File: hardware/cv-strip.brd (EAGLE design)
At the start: 152.5 x 43.6 mm, 118 parts, among them IC1 PIC16F1825SO14, IC2 AD5696R, IC3 MC14094B, IC4 MC14094B, IC5 LM324D, IC6 REG1117, IC7 6N138

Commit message: Final rev 2 release PCB
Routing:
- net GND: vias 7 -> 8
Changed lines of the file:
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@@
 </class>
 </classes>
-<designrules name="ITEADstudio_DRC">
-<description language="de">&lt;b&gt;EAGLE Design Rules&lt;/b&gt;
-&lt;p&gt;
-Die Standard-Design-Rules sind so gewählt, dass sie für
-die meisten Anwendungen passen. Sollte ihre Platine
-besondere Anforderungen haben, treffen Sie die erforderlichen
-Einstellungen hier und speichern die Design Rules unter
-einem neuen Namen ab.</description>
-<description language="en">&lt;b&gt;EAGLE Design Rules&lt;/b&gt;
-&lt;p&gt;
-The default Design Rules have been set to cover
-a wide range of applications. Your particular design
-may have different requirements, so please make the
-necessary adjustments and save your customized
-design rules under a new name.</description>
-<description language="zh">&lt;b&gt;Seeed Studio EAGLE Design Rules&lt;/b&gt;
-</description>
+<designrules name="dirt_cheap_dirty_boards.v1">
+<description language="en">&lt;b&gt;Dirty Cheap Dirty Board Design Rules&lt;/b&gt;
+&lt;br&gt;
+&lt;br&gt;Min width/Spacing: 5/5mil
+&lt;br&gt;Min diameter of finished hole 12mil</description>
 <param name="layerSetup" value="(1*16)"/>
-<param name="mtCopper" value="0.035mm 0.035mm 0.035mm 0.035mm 0.035mm 0.035mm 0.035mm 0.035mm 0.035mm 0.035mm 0.035mm 0.035mm 0.035mm 0.035mm 0.035mm 0.035mm"/>
-<param name="mtIsolate" value="1.5mm 0.15mm 0.2mm 0.15mm 0.2mm 0.15mm 0.2mm 0.15mm 0.2mm 0.15mm 0.2mm 0.15mm 0.2mm 0.15mm 0.2mm"/>
-<param name="mdWireWire" value="6mil"/>
-<param name="mdWirePad" value="6mil"/>
-<param name="mdWireVia" value="6mil"/>
-<param name="mdPadPad" value="6mil"/>
-<param name="mdPadVia" value="6mil"/>
-<param name="mdViaVia" value="6mil"/>
+<param name="mtCopper" value="0.035mm 0.0175mm 0.035mm 0.035mm 0.035mm 0.035mm 0.035mm 0.035mm 0.035mm 0.035mm 0.035mm 0.035mm 0.035mm 0.035mm 0.0175mm 0.035mm"/>
+<param name="mtIsolate" value="1.5mm 1.1mm 0.2mm 0.15mm 0.2mm 0.15mm 0.2mm 0.15mm 0.2mm 0.15mm 0.2mm 0.15mm 0.2mm 0.15mm 0.2mm"/>
+<param name="mdWireWire" value="5mil"/>
+<param name="mdWirePad" value="5mil"/>
+<param name="mdWireVia" value="5mil"/>
+<param name="mdPadPad" value="5mil"/>
+<param name="mdPadVia" value="5mil"/>
+<param name="mdViaVia" value="5mil"/>
 <param name="mdSmdPad" value="0mil"/>
 <param name="mdSmdVia" value="0mil"/>
@@
 <param name="mdDrill" value="10mil"/>
 <param name="mdSmdStop" value="0mil"/>
-<param name="msWidth" value="6mil"/>
+<param name="msWidth" value="5mil"/>
 <param name="msDrill" value="12mil"/>
 <param name="msMicroVia" value="12mil"/>
@@
 <param name="mlMinCreamFrame" value="0mil"/>
 <param name="mlMaxCreamFrame" value="0mil"/>
-<param name="mlViaStopLimit" value="100mil"/>
+<param name="mlViaStopLimit" value="25mil"/>
 <param name="srRoundness" value="0"/>
 <param name="srMinRoundness" value="0mil"/>
@@
 <wire x1="66.675" y1="26.7995" x2="68.0525" y2="26.7995" width="0.4064" layer="16"/>
 <wire x1="68.0525" y1="26.7995" x2="69.088" y2="27.327" width="0.4064" layer="16"/>
-<wire x1="91.302" y1="14.49" x2="93.102" y2="15.99" width="0" layer="19" extent="16-16"/>
-<wire x1="98.944" y1="15.99" x2="97.144" y2="14.49" width="0" layer="19" extent="16-16"/>
+<via x="98.8695" y="18.161" extent="1-16" drill="0.6"/>
 </signal>
 <signal name="MIDI_IN">
@@
 <via x="49.53" y="33.02" extent="1-16" drill="0.6"/>
 <contactref element="C16" pad="+"/>
-<wire x1="60.35" y1="31.9405" x2="64.0105" y2="31.9405" width="0.3048" layer="16"/>
+<wire x1="60.35" y1="31.9405" x2="63.5" y2="31.9405" width="0.3048" layer="16"/>
+<wire x1="64.008" y1="31.9405" x2="64.0105" y2="31.9405" width="0.3048" layer="16"/>
 <wire x1="64.0715" y1="32.004" x2="64.0715" y2="30.9245" width="0.6096" layer="16"/>
 <wire x1="64.0715" y1="30.9245" x2="64.5795" y2="30.4165" width="0.6096" layer="16"/>
@@
 <wire x1="138.43" y1="7.112" x2="137.342" y2="7.112" width="0.6096" layer="16"/>
 <wire x1="137.342" y1="7.112" x2="137.16" y2="6.93" width="0.6096" layer="16"/>
-<wire x1="64.008" y1="31.9405" x2="64.0105" y2="31.9405" width="0" layer="19" extent="16-16"/>
+<wire x1="64.008" y1="31.9405" x2="63.5" y2="31.9405" width="0.4064" layer="16"/>
 </signal>
 <signal name="VIN">

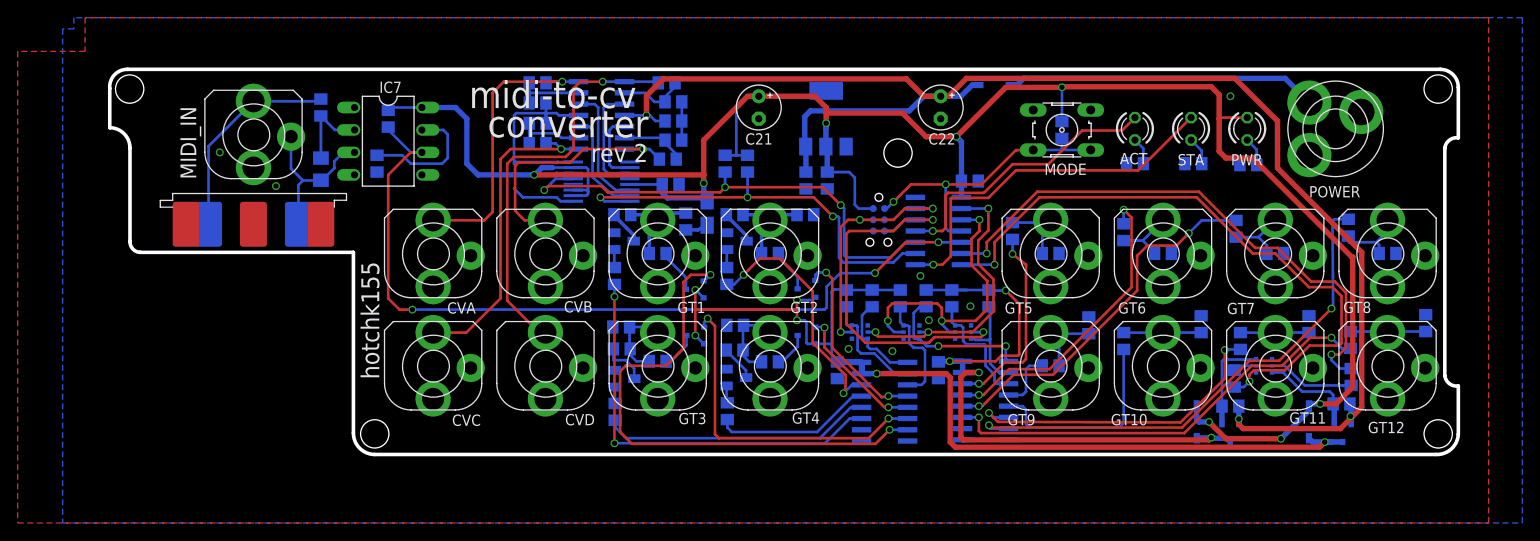
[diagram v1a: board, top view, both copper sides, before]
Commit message: REV2A
fixed some DRC issues
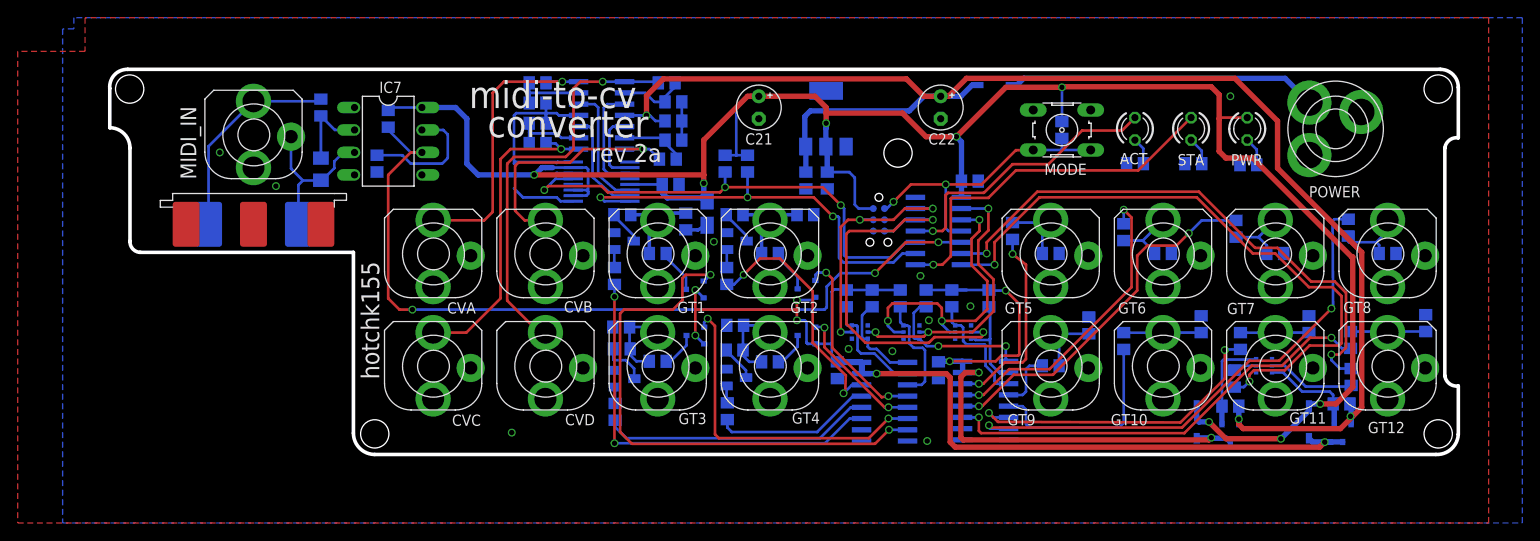
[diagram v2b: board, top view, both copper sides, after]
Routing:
- net GT1H: track 60.8 -> 61.7 mm
- net GND: vias 8 -> 11
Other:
- board text added: "rev 2a"
- board text removed: "rev 2"
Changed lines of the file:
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@@
 <text x="42.164" y="40.5765" size="3.048" layer="25" font="vector">midi-to-cv </text>
 <text x="44.2595" y="37.2745" size="3.048" layer="25" font="vector">converter</text>
-<text x="55.9435" y="34.4805" size="2.032" layer="25" font="vector">rev 2</text>
+<text x="55.9435" y="34.4805" size="2.032" layer="25" font="vector">rev 2a</text>
 <text x="32.004" y="9.906" size="2.032" layer="25" font="vector" rot="R90">hotchk155</text>
 <hole x="90.678" y="35.488" drill="3.2"/>
@@
 </class>
 </classes>
-<designrules name="dirt_cheap_dirty_boards.v1">
-<description language="en">&lt;b&gt;Dirty Cheap Dirty Board Design Rules&lt;/b&gt;
-&lt;br&gt;
-&lt;br&gt;Min width/Spacing: 5/5mil
-&lt;br&gt;Min diameter of finished hole 12mil</description>
+<designrules name="hackvana">
+<description language="de">&lt;b&gt;EAGLE Design Rules für Hackvana&lt;/b&gt;
+&lt;p&gt;
+Die Standard-Design-Rules sind so gewählt, dass sie für
+die meisten Anwendungen passen. Sollte ihre Platine
+besondere Anforderungen haben, treffen Sie die erforderlichen
+Einstellungen hier und speichern die Design Rules unter
+einem neuen Namen ab.</description>
+<description language="en">&lt;b&gt;EAGLE Design Rules for Hackvana&lt;/b&gt;
+&lt;p&gt;
+The default Design Rules have been set to cover
+a wide range of applications. Your particular design
+may have different requirements, so please make the
+necessary adjustments and save your customized
+design rules under a new name.</description>
+<description language="zh">&lt;b&gt;EAGLE Design Rules for Hackvana&lt;/b&gt;
+</description>
 <param name="layerSetup" value="(1*16)"/>
-<param name="mtCopper" value="0.035mm 0.0175mm 0.035mm 0.035mm 0.035mm 0.035mm 0.035mm 0.035mm 0.035mm 0.035mm 0.035mm 0.035mm 0.035mm 0.035mm 0.0175mm 0.035mm"/>
-<param name="mtIsolate" value="1.5mm 1.1mm 0.2mm 0.15mm 0.2mm 0.15mm 0.2mm 0.15mm 0.2mm 0.15mm 0.2mm 0.15mm 0.2mm 0.15mm 0.2mm"/>
-<param name="mdWireWire" value="5mil"/>
-<param name="mdWirePad" value="5mil"/>
-<param name="mdWireVia" value="5mil"/>
-<param name="mdPadPad" value="5mil"/>
-<param name="mdPadVia" value="5mil"/>
-<param name="mdViaVia" value="5mil"/>
+<param name="mtCopper" value="0.035mm 0.035mm 0.035mm 0.035mm 0.035mm 0.035mm 0.035mm 0.035mm 0.035mm 0.035mm 0.035mm 0.035mm 0.035mm 0.035mm 0.035mm 0.035mm"/>
+<param name="mtIsolate" value="1.5mm 0.15mm 0.2mm 0.15mm 0.2mm 0.15mm 0.2mm 0.15mm 0.2mm 0.15mm 0.2mm 0.15mm 0.2mm 0.15mm 0.2mm"/>
+<param name="mdWireWire" value="6mil"/>
+<param name="mdWirePad" value="9mil"/>
+<param name="mdWireVia" value="6mil"/>
+<param name="mdPadPad" value="6mil"/>
+<param name="mdPadVia" value="6mil"/>
+<param name="mdViaVia" value="6mil"/>
 <param name="mdSmdPad" value="0mil"/>
 <param name="mdSmdVia" value="0mil"/>
@@
 <param name="mdViaViaSameLayer" value="8mil"/>
 <param name="mnLayersViaInSmd" value="2"/>
-<param name="mdCopperDimension" value="10mil"/>
-<param name="mdDrill" value="10mil"/>
+<param name="mdCopperDimension" value="6mil"/>
+<param name="mdDrill" value="6mil"/>
 <param name="mdSmdStop" value="0mil"/>
-<param name="msWidth" value="5mil"/>
-<param name="msDrill" value="12mil"/>
-<param name="msMicroVia" value="12mil"/>
+<param name="msWidth" value="6mil"/>
+<param name="msDrill" value="0.3mm"/>
+<param name="msMicroVia" value="0.25mm"/>
 <param name="msBlindViaRatio" value="0.5"/>
 <param name="rvPadTop" value="0.25"/>
@@
 <param name="mlMinCreamFrame" value="0mil"/>
 <param name="mlMaxCreamFrame" value="0mil"/>
-<param name="mlViaStopLimit" value="25mil"/>
+<param name="mlViaStopLimit" value="100mil"/>
 <param name="srRoundness" value="0"/>
 <param name="srMinRoundness" value="0mil"/>
@@
 <wire x1="68.0525" y1="26.7995" x2="69.088" y2="27.327" width="0.4064" layer="16"/>
 <via x="98.8695" y="18.161" extent="1-16" drill="0.6"/>
+<via x="69.85" y="25.4635" extent="1-16" drill="0.6"/>
+<via x="46.99" y="3.8735" extent="1-16" drill="0.6"/>
+<via x="93.98" y="2.921" extent="1-16" drill="0.6"/>
 </signal>
 <signal name="MIDI_IN">
@@
 <contactref element="Q3" pad="2"/>
 <wire x1="132.98" y1="11.43" x2="134.4295" y2="11.43" width="0.3048" layer="16"/>
-<wire x1="134.4295" y1="11.43" x2="136.652" y2="9.2075" width="0.3048" layer="16"/>
-<wire x1="136.652" y1="9.2075" x2="140.9675" y2="9.2075" width="0.3048" layer="16"/>
-<wire x1="140.9675" y1="9.2075" x2="141.9225" y2="9.21" width="0.3048" layer="16"/>
+<wire x1="134.4295" y1="11.43" x2="136.779" y2="9.0805" width="0.3048" layer="16"/>
+<wire x1="136.779" y1="9.0805" x2="141.793" y2="9.0805" width="0.3048" layer="16"/>
+<wire x1="141.793" y1="9.0805" x2="141.9225" y2="9.21" width="0.3048" layer="16"/>
 </signal>
 <signal name="N$47">
@@
 <wire x1="68.768" y1="21.016" x2="69.469" y2="21.717" width="0.3048" layer="16"/>
 <via x="69.469" y="21.717" extent="1-16" drill="0.6"/>
-<wire x1="69.469" y1="21.717" x2="67.2465" y2="21.717" width="0.3048" layer="1"/>
-<wire x1="67.2465" y1="21.717" x2="66.421" y2="20.8915" width="0.3048" layer="1"/>
-<wire x1="66.421" y1="20.8915" x2="66.421" y2="13.3985" width="0.3048" layer="1"/>
-<wire x1="66.421" y1="13.3985" x2="64.4525" y2="11.43" width="0.3048" layer="1"/>
-<wire x1="64.4525" y1="11.43" x2="59.8805" y2="11.43" width="0.3048" layer="1"/>
-<wire x1="59.8805" y1="11.43" x2="59.2455" y2="10.795" width="0.3048" layer="1"/>
-<wire x1="59.2455" y1="10.795" x2="59.2455" y2="3.937" width="0.3048" layer="1"/>
-<via x="89.7255" y="4.191" extent="1-16" drill="0.6"/>
-<wire x1="89.7255" y1="4.191" x2="91.754" y2="4.191" width="0.3048" layer="16"/>
-<wire x1="88.138" y1="2.6035" x2="60.579" y2="2.6035" width="0.3048" layer="1"/>
+<wire x1="59.2455" y1="17.3355" x2="59.2455" y2="3.937" width="0.3048" layer="1"/>
+<via x="89.662" y="4.191" extent="1-16" drill="0.6"/>
+<wire x1="89.662" y1="4.191" x2="91.754" y2="4.191" width="0.3048" layer="16"/>
+<wire x1="88.0745" y1="2.6035" x2="60.579" y2="2.6035" width="0.3048" layer="1"/>
 <wire x1="60.579" y1="2.6035" x2="59.2455" y2="3.937" width="0.3048" layer="1"/>
-<wire x1="88.138" y1="2.6035" x2="89.7255" y2="4.191" width="0.3048" layer="1"/>
+<wire x1="88.0745" y1="2.6035" x2="89.662" y2="4.191" width="0.3048" layer="1"/>
+<wire x1="59.2455" y1="17.3355" x2="59.69" y2="17.78" width="0.3048" layer="1"/>
+<wire x1="59.69" y1="17.78" x2="65.2145" y2="17.78" width="0.3048" layer="1"/>
+<wire x1="65.2145" y1="17.78" x2="66.294" y2="18.8595" width="0.3048" layer="1"/>
+<wire x1="66.294" y1="18.8595" x2="66.294" y2="21.336" width="0.3048" layer="1"/>
+<wire x1="66.294" y1="21.336" x2="66.675" y2="21.717" width="0.3048" layer="1"/>
+<wire x1="66.675" y1="21.717" x2="69.469" y2="21.717" width="0.3048" layer="1"/>
 </signal>
 <signal name="GT1L">
@@
 <contactref element="Q8" pad="C"/>
 <wire x1="71.2495" y1="28.5115" x2="71.2495" y2="28.4455" width="0.4064" layer="16"/>
-<wire x1="71.2495" y1="28.4455" x2="73.5535" y2="26.1415" width="0.4064" layer="16"/>
-<wire x1="73.5535" y1="25.527" x2="73.5535" y2="26.1415" width="0.4064" layer="16"/>
+<wire x1="71.2495" y1="28.4455" x2="73.5535" y2="26.1415" width="0.3048" layer="16"/>
+<wire x1="73.5535" y1="25.527" x2="73.5535" y2="26.1415" width="0.3048" layer="16"/>
 </signal>
 <signal name="N$51">
@@
 <contactref element="R47" pad="1"/>
 <wire x1="58.5495" y1="28.5115" x2="58.5495" y2="28.4455" width="0.4064" layer="16"/>
-<wire x1="58.5495" y1="28.4455" x2="60.833" y2="26.162" width="0.4064" layer="16"/>
-<wire x1="60.833" y1="26.162" x2="60.833" y2="25.57" width="0.4064" layer="16"/>
 <wire x1="60.833" y1="25.57" x2="60.79" y2="25.527" width="0.4064" layer="16"/>
+<wire x1="58.5495" y1="28.4455" x2="58.5495" y2="28.382" width="0.3048" layer="16"/>
+<wire x1="58.5495" y1="28.382" x2="60.833" y2="26.0985" width="0.3048" layer="16"/>
+<wire x1="60.833" y1="26.0985" x2="60.833" y2="25.57" width="0.3048" layer="16"/>
 </signal>
 </signals>

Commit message: working on rev 3 LPC812
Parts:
- removed Q3, Q4, Q5, Q6: (no value), microbuilder:SOT363
- added C23: 100n, rcl:C0805
- added C24, C25: (no value), rcl:C0805
- added IC8: 24LC_64T-I/OT, Microchip-24LCxxx:SOT95P290X145-5N
- added IC9: MIC5504-2.8YM5-TR, jason_eagle6:SOT23-5
- added Q15, Q16, Q17, Q18: (no value), jason_eagle6:SOT363
- IC1: value PIC16F1825SO14 -> LPC812; device jasons_stuff:SO14 -> jason_eagle6:TSSOP20
- moved C9 34.2 mm to (64.6, 31.9)
- moved R38 27.6 mm to (123.9, 31.1), turned to 0 degrees
- moved R39 21.2 mm to (130.0, 31.1), turned to 180 degrees
- moved C15 20.7 mm to (85.3, 28.1), turned to 90 degrees
- moved R4 10.7 mm to (100.3, 32.2)
- moved ICSP 10.3 mm to (98.6, 28.5)
- moved IC1 3.81 mm to (91.4, 26.7)
- moved R6 2.27 mm to (128.4, 16.3), turned to 270 degrees
- moved R34 1.27 mm to (99.7, 19.1)
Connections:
- net VIN renamed 12V
- removed net N$22: Q3.2, R38.2
- removed net N$47: Q3.5, R39.2
- removed net VDD: C10.1, C15.2, C16.+, C21.+, C9.2, D3.A, D4.A, IC1.1, IC2.P$10, IC2.P$11, IC2.P$15, IC2.P$5, IC6.2, IC7.8, ICSP.2, PWR.A, R21.1, R22.1, R27.2, R4.1
- new net 3V3: C15.1, C24.2, IC1.15, IC9.5, ICSP.2, PWR.A, R4.1
- new net 5V: C10.1, C16.+, C21.+, C23.1, C25.2, C9.2, D3.A, D4.A, IC2.P$10, IC2.P$11, IC2.P$15, IC2.P$5, IC6.2, IC7.8, IC8.4, IC9.1, IC9.3, R21.1, R22.1, R27.2, R38.2, R39.2
- new net MODE_SW: IC1.1, MODE.1, MODE.2
- new net N$57: IC1.7, ICSP.4
- new net N$58: IC1.4, ICSP.1, R4.2
- net ACT_LED: now also IC1.2; no longer IC1.11
- net GND: now also C15.2, C23.2, C24.1, C25.1, IC1.16, IC8.2, IC8.5, IC9.2, Q15.1, Q15.4, Q16.1, Q16.4, Q17.1, Q17.4, Q18.1, Q18.4; no longer C15.1, IC1.14, Q3.1, Q3.4, Q4.1, Q4.4, Q5.1, Q5.4, Q6.1, Q6.4
- net GT1_VSEL: now also IC1.10, Q18.5; no longer IC1.6
- net GT2_VSEL: now also IC1.17, Q18.2; no longer IC1.7
- net N$14: now also Q15.3; no longer Q6.3
- net N$15: now also Q15.6; no longer Q6.6
- net N$16: now also Q16.6; no longer Q5.6
- net N$21: now also Q18.6; no longer Q3.6
- net N$34: now also IC1.6, ICSP.5; no longer IC1.4, ICSP.1, MODE.1, MODE.2, R4.2
- net N$48: now also Q16.3; no longer Q5.3
- net N$49: now also Q17.3; no longer Q4.3
- net N$50: now also Q17.6; no longer Q4.6
- net N$9: now also Q18.3; no longer Q3.3
- net SCL: now also IC1.8, IC8.1; no longer IC1.10
- net SDA: now also IC8.3
- net SR_CLK: now also IC1.11, Q16.2, Q17.2; no longer IC1.3, Q4.5, Q5.5
- net SR_DAT: now also Q15.2; no longer ICSP.4, Q6.5
- net SR_DAT2: now also Q17.5; no longer ICSP.5, Q4.2
- net SR_RCK: now also IC1.14, Q15.5, Q16.5; no longer IC1.2, Q5.2, Q6.2
- net STATUS_LED: now also IC1.3; no longer IC1.8
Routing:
- net 5V: track 0.00 -> 257.0 mm, vias 0 -> 8
- net VDD: track 243.5 -> 0.00 mm, vias 8 -> 0
- net 3V3: track 0.00 -> 78.8 mm, vias 0 -> 2
- net N$34: track 34.7 -> 7.73 mm
- net SR_DAT2: track 45.0 -> 18.2 mm
- net MODE_SW: track 0.00 -> 21.1 mm, vias 0 -> 1
- net SR_DAT: track 27.9 -> 14.5 mm, vias 3 -> 2
- net SR_CLK: track 33.3 -> 20.3 mm
- net 12V: track 168.6 -> 156.5 mm, vias 3 -> 4
- net SDA: track 48.1 -> 59.4 mm, vias 3 -> 4
- net N$58: track 0.00 -> 11.2 mm, vias 0 -> 2
- net N$22: track 9.97 -> 0.00 mm
- net SR_RCK: track 32.6 -> 23.2 mm
- net STATUS_LED: track 41.9 -> 34.2 mm
- net N$44: track 36.6 -> 42.6 mm
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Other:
- board text added: "rev 3"
- board text removed: "rev 2a"

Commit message: mods
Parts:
- renumbered Q15 to Q6, Q16 to Q5, Q17 to Q4, Q18 to Q3
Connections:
- net MIDI_IN: now also IC1.19; no longer IC1.5
- net STATUS_LED: now also IC1.20; no longer IC1.3
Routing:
- net STATUS_LED: track 34.2 -> 39.4 mm
- net MIDI_IN: track 92.4 -> 96.4 mm, vias 1 -> 3
- net GT2_VSEL: track 71.3 -> 71.8 mm
